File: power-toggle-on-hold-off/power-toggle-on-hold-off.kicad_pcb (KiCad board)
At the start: 2 copper layers, 16.5 x 19 mm, 13 parts, among them J1 VIN, SW1 POWER, U1 BSD235C

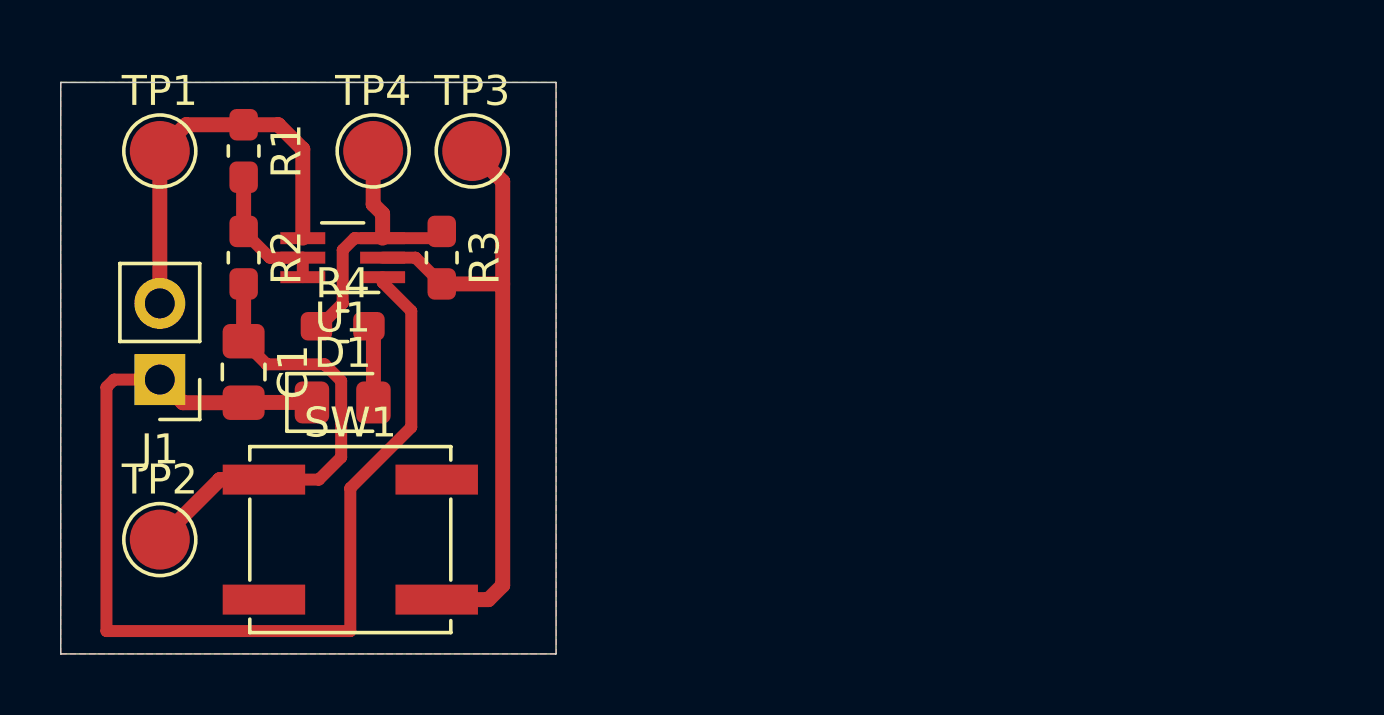
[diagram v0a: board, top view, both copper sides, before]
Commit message: Updated on-off schematics for verification, last one did not work :-)
Signed-off-by: Tomasz 'CeDeROM' CEDRO <tomek@cedro.info>
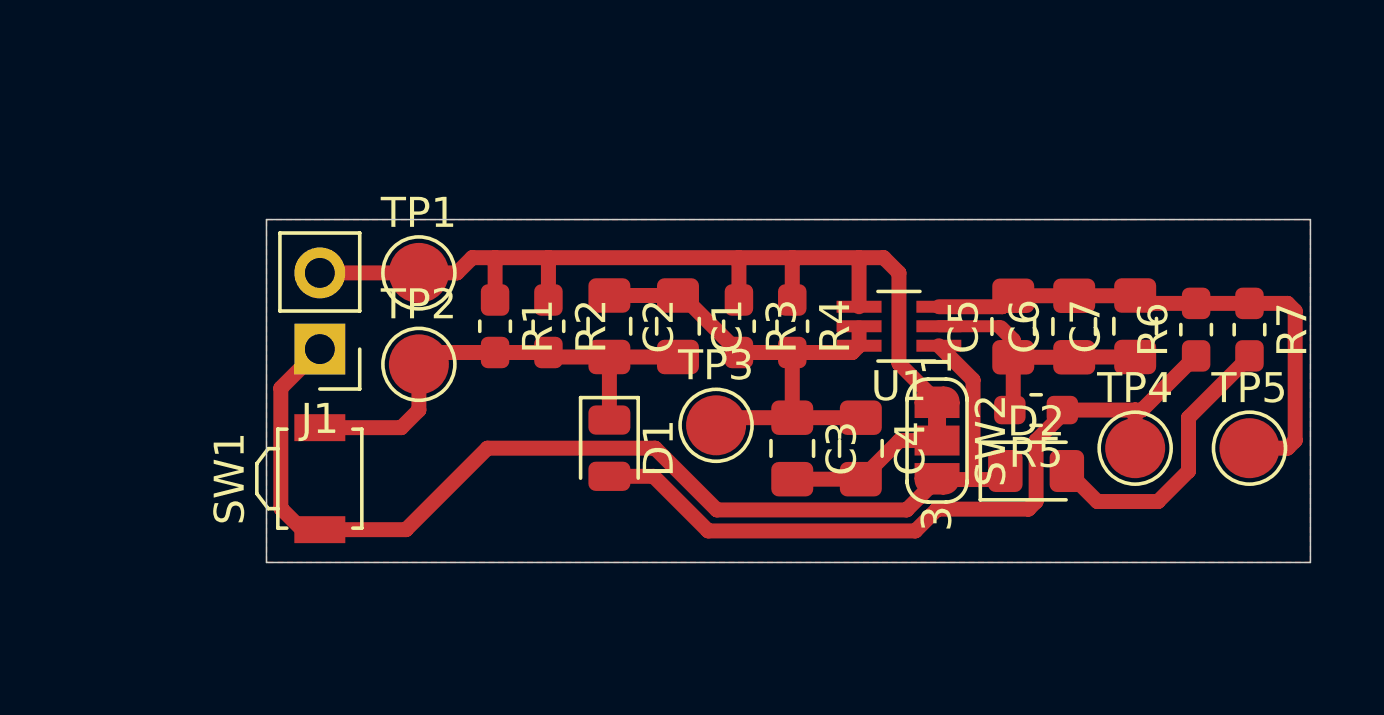
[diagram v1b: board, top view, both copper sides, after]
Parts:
- added C2: ???, Capacitor_SMD:C_0805_2012Metric_Pad1.15x1.40mm_HandSolder, F.Cu at (67.8, 39.9)
- added C3: 100nF, Capacitor_SMD:C_0805_2012Metric_Pad1.15x1.40mm_HandSolder, F.Cu at (73.9, 44.0)
- added C4: ???, Capacitor_SMD:C_0805_2012Metric_Pad1.15x1.40mm_HandSolder, F.Cu at (76.2, 44.0)
- added C5: 1uF, Capacitor_SMD:C_0805_2012Metric_Pad1.15x1.40mm_HandSolder, F.Cu at (81.3, 39.9)
- added C6: 10uF, Capacitor_SMD:C_0805_2012Metric_Pad1.15x1.40mm_HandSolder, F.Cu at (83.3, 39.9)
- added C7: ???, Capacitor_SMD:C_0805_2012Metric_Pad1.15x1.40mm_HandSolder, F.Cu at (85.3, 39.9)
- added D2: LED, Diode_SMD:D_0805_2012Metric_Pad1.15x1.40mm_HandSolder, F.Cu at (82.0, 44.7)
- added R5: 300K, Resistor_SMD:R_0603_1608Metric_Pad1.05x0.95mm_HandSolder, F.Cu at (82.0, 42.7)
- added R6: 100K, Resistor_SMD:R_0603_1608Metric_Pad1.05x0.95mm_HandSolder, F.Cu at (87.4, 40.0)
- added R7: 220R, Resistor_SMD:R_0603_1608Metric_Pad1.05x0.95mm_HandSolder, F.Cu at (89.2, 40.0)
- added SW2: POWERONDEF, Jumper:SolderJumper-3_P1.3mm_Bridged12_RoundedPad1.0x1.5mm_NumberLabels, F.Cu at (78.7, 43.7)
- added TP5: VOUT, TestPoint:TestPoint_Pad_D2.0mm, F.Cu at (89.2, 43.9)
- C1: value 10uF -> 1uF
- D1: value LED -> 1N4148; footprint Diode_SMD:D_0805_2012Metric_Pad1.15x1.40mm_HandSolder -> Diode_SMD:D_0805_2012Metric
- R1: value 10K -> 10k
- R2: value 100K -> ???
- R3: value 10K -> ???
- R4: value 220R -> 100k
- SW1: footprint Button_Switch_SMD:SW_SPST_EVQP0 -> Button_Switch_SMD:SW_SPST_B3U-3000P
- TP3: value BUTTON -> VGD
- TP4: value VOUT -> PWRCTL
- moved TP4 27.3 mm to (85.3, 43.9)
- moved U1 18.7 mm to (77.5, 39.9)
- moved R4 15.0 mm to (73.9, 39.9), turned to 270 degrees
- moved C1 14.6 mm to (70.1, 39.9)
- moved TP3 12.2 mm to (71.4, 43.2)
- moved TP2 10.4 mm to (61.5, 41.1)
- moved R2 10.4 mm to (65.8, 39.9)
- moved R1 10.2 mm to (64.0, 39.9)
- moved R3 10.2 mm to (72.1, 39.9)
- moved TP1 9.54 mm to (61.5, 38.1)
- moved D1 9.02 mm to (67.8, 43.9), turned to 270 degrees
- moved J1 5.43 mm to (58.2, 40.6)
- moved SW1 2.27 mm to (58.2, 45.0), turned to 90 degrees
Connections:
- C1 pad 2: GND -> Net-(C1-Pad2)
- D1 pad 1: GND -> Net-(C1-Pad2)
- R1 pad 2: Net-(R1-Pad2) -> Net-(C1-Pad2)
- R2 pad 1: Net-(R1-Pad2) -> VCC
- R2 pad 2: Net-(C1-Pad1) -> Net-(C1-Pad2)
- R3 pad 1: Net-(R3-Pad1) -> VCC
- R3 pad 2: Net-(R3-Pad2) -> Net-(C1-Pad1)
- R4 pad 1: Net-(R3-Pad1) -> VCC
- R4 pad 2: Net-(D1-Pad2) -> Net-(C1-Pad1)
- SW1 pad 1: Net-(C1-Pad1) -> GND
- SW1 pad 2: Net-(R3-Pad2) -> Net-(C1-Pad2)
- TP2 pad 1: Net-(C1-Pad1) -> Net-(C1-Pad2)
- TP3 pad 1: Net-(R3-Pad2) -> Net-(C1-Pad1)
- TP4 pad 1: Net-(R3-Pad1) -> Net-(D1-Pad2)
- U1 pad 2: Net-(R3-Pad2) -> Net-(C5-Pad1)
- U1 pad 3: Net-(R3-Pad1) -> Net-(C5-Pad2)
- U1 pad 5: Net-(R1-Pad2) -> Net-(C1-Pad1)
- U1 pad 6: Net-(R1-Pad2) -> Net-(C1-Pad1)
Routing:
- net Net-(D1-Pad2): track 2.60 -> 25.3 mm
- net Net-(R3-Pad2): track 21.7 -> 0.00 mm
- net VCC: track 13.5 -> 31.8 mm
- net Net-(C5-Pad2): track 0.00 -> 18.2 mm
- net Net-(C1-Pad2): track 0.00 -> 16.0 mm
- net Net-(D2-Pad2): track 0.00 -> 9.58 mm
- net Net-(R3-Pad1): track 9.56 -> 0.00 mm
- net Net-(C5-Pad1): track 0.00 -> 9.12 mm
- net Net-(C3-Pad2): track 0.00 -> 5.36 mm
- net Net-(R1-Pad2): track 4.79 -> 0.00 mm
- net Net-(C1-Pad1): track 15.4 -> 16.9 mm
- net GND: track 36.6 -> 37.7 mm
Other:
- board size 16.5 x 19 mm -> 34.8 x 11.4 mm
